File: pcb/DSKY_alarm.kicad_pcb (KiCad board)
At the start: 4 copper layers, 57.8 x 101.6 mm, 88 parts, among them IC3 ATSAMD21E, SW1 reset, U1 AQY232SZ, U10 AQY232SZ, U11 AQY232SZ, U12 AQY232SZ, U13 AQY232SZ, U14 AQY232SZ, U15 AP2112K-3.3, U2 AQY232SZ, U3 AQY232SZ, U4 AQY232SZ, U5 AQY232SZ, U6 AQY232SZ, U7 AQY232SZ, U8 AQY232SZ, X1 USB_MICRO_20329_V2_revised, u9 AQY232SZ

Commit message: Version 4 of the board
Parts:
- added NT1: Net-Tie_2, NetTie:NetTie-2_SMD_Pad0.5mm, F.Cu at (109.2, 146.7)
- LA11, LA12, LA13, LA21, LA22, LA23, LA31, LA32, LA33, LA41, LA42, LA43, LA51, LA52, LA53, LA61, LA62, LA63, LA71, LA72, LA73, LA81, LA82, LA83, LA91, LA92, LA93, LAA1, LAA2, LAA3, LAB1, LAB2, LAB3, LAC1, LAC2, LAC3, LAD1, LAD2, LAD3, LAE1, LAE2, LAE3: footprint Trinket M0 rev D:VCC7216-ND -> Trinket M0 rev D:VCC7265
- X1: value USB_MICRO_20329_V2_revised -> Molex 105133 USB; footprint Trinket M0 rev D:4UCONN_20329_V2_revised -> libraries:MOLEX_105133-0001
- moved X1 66.8 mm to (109.2, 138.4), turned to 0 degrees
- moved REF** 23.7 mm to (109.2, 130.8)
- moved R7 3.24 mm to (118.9, 135.3)
- moved U7 3.24 mm to (126.4, 136.5)
- moved R14 2.54 mm to (101.6, 135.9), turned to 180 degrees
- moved U14 2.54 mm to (94.0, 137.2)
- moved SWC1 1.27 mm to (87.6, 108.6)
- moved SWD1 1.27 mm to (84.5, 108.6)
- moved LA12 0.64 mm to (123.8, 53.3)
- moved LA42 0.64 mm to (123.8, 99.1)
- moved LA52 0.64 mm to (123.8, 114.3)
- moved LA62 0.64 mm to (123.8, 129.5)
- moved LA83 0.64 mm to (85.1, 53.3)
- moved LA93 0.64 mm to (85.1, 68.6)
- moved LAB3 0.64 mm to (85.1, 99.1)
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- renumbered u9 to U9
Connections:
- net +5V renamed VBAT
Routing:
- net VBUS: track 42.2 -> 81.6 mm, vias 2 -> 3
- net VBAT: track 539.1 -> 573.0 mm
- net GND: track 390.8 -> 415.0 mm, vias 0 -> 3
- net /D-: track 49.2 -> 30.4 mm, vias 2 -> 0
- net /D+: track 47.4 -> 29.7 mm, vias 2 -> 0
- net Net-(IC3-Pad31): track 37.6 -> 26.8 mm
- net LA6_PA22: track 32.9 -> 24.2 mm, vias 0 -> 2
- net LA5_PA19: track 26.3 -> 32.3 mm, vias 0 -> 2
- net LA3_PA04: track 20.7 -> 26.1 mm
- net Net-(IC3-Pad32): track 36.1 -> 32.1 mm
- net LA2_PA03: track 53.9 -> 56.8 mm, vias 2 -> 3
- net Net-(R6-Pad2): track 7.85 -> 5.10 mm, vias 2 -> 0
- net LA1_PA02: track 53.3 -> 50.5 mm
- net LA11_PA15: track 20.5 -> 18.0 mm
- net LA14_PA18: track 33.0 -> 30.7 mm, vias 2 -> 0
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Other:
- board text added: "DSKY Alarm Indicator, V4.0"
- board text removed: "DSKY Alarm Indicator, V3.0"

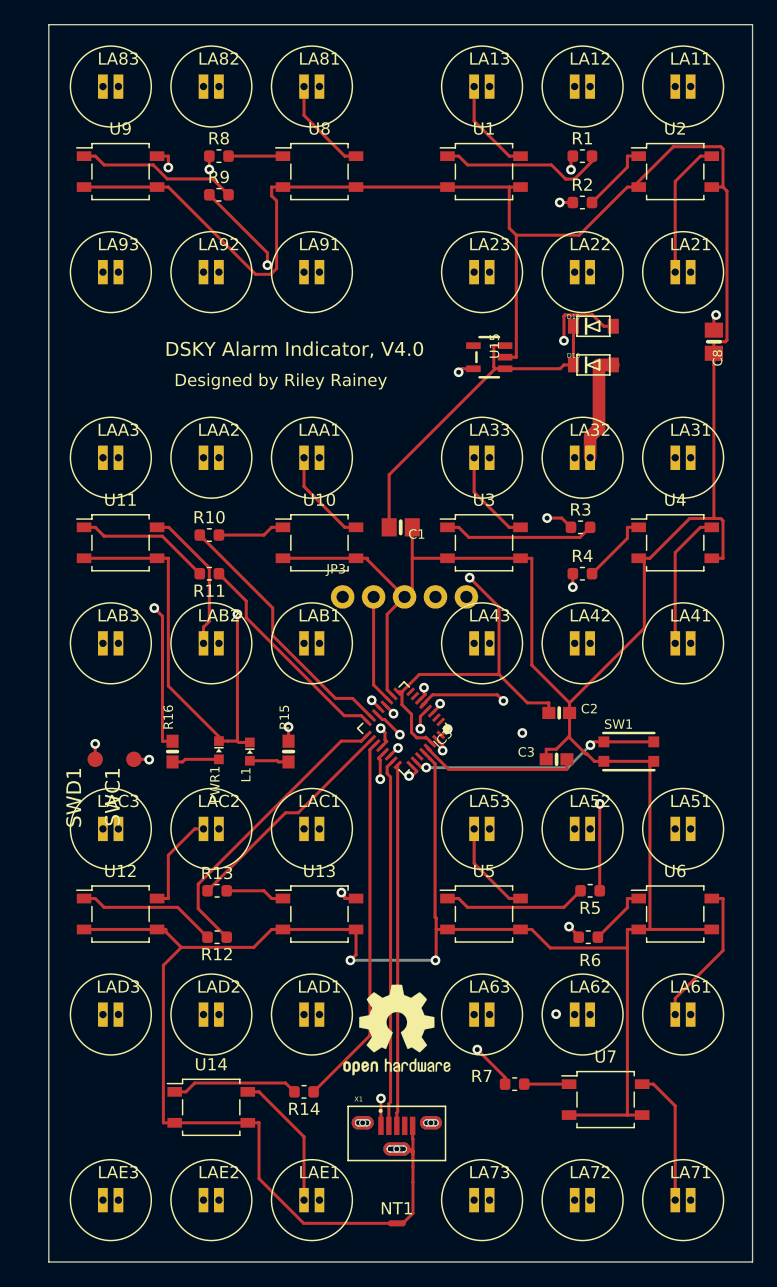
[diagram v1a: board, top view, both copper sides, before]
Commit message: Updated V4 board to a two layer design
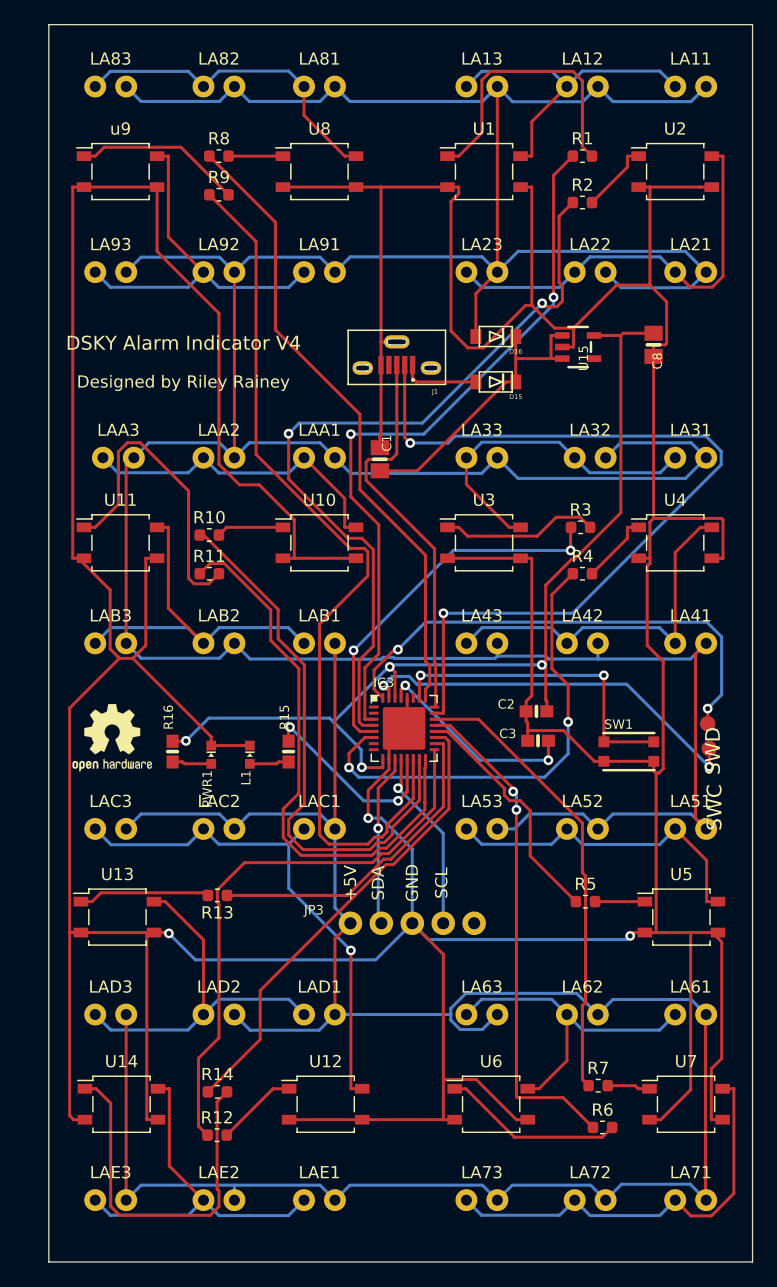
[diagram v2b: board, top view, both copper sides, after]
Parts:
- removed NT1: Net-Tie_2, NetTie:NetTie-2_SMD_Pad0.5mm
- removed the REF** at (109.2, 130.8)
- removed X1: Molex 105133 USB, libraries:MOLEX_105133-0001
- added J1: 105133-0001-MOLEX-USB, libraries:MOLEX_105133-0001, F.Cu at (109.2, 76.5)
- added REF**: OSHW-Logo2_7.3x6mm_SilkScreen, Symbol:OSHW-Logo2_7.3x6mm_SilkScreen, F.Cu at (85.9, 106.8)
- LA11, LA12, LA13, LA21, LA22, LA23, LA31, LA32, LA33, LA41, LA42, LA43, LA51, LA52, LA53, LA61, LA62, LA63, LA71, LA72, LA73, LA81, LA82, LA83, LA91, LA92, LA93, LAA1, LAA2, LAA3, LAB1, LAB2, LAB3, LAC1, LAC2, LAC3, LAD1, LAD2, LAD3, LAE1, LAE2, LAE3: footprint Trinket M0 rev D:VCC7265 -> Trinket M0 rev D:VCC7216-ND
- moved SWD 50.4 mm to (134.7, 105.7)
- moved SWC 47.3 mm to (134.9, 107.7)
- moved JP3 26.8 mm to (110.5, 122.0)
- moved U12 23.0 mm to (103.4, 136.9)
- moved U6 21.7 mm to (117.0, 136.9)
- moved U13 16.6 mm to (86.3, 121.5)
- moved R12 16.3 mm to (94.5, 139.4), turned to 0 degrees
- moved U5 16.2 mm to (132.6, 121.5)
- moved R6 15.7 mm to (126.1, 138.8)
- moved D15 9.23 mm to (117.3, 77.6), turned to 180 degrees
- moved D16 8.35 mm to (117.3, 73.9), turned to 180 degrees
- moved U14 7.37 mm to (86.6, 136.9)
- moved U15 7.35 mm to (124.1, 74.7), turned to 270 degrees
- moved R14 7.11 mm to (94.5, 135.9), turned to 0 degrees
- moved R7 6.86 mm to (125.8, 135.4)
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- renumbered SWC1 to SWC, SWD1 to SWD, U9 to u9
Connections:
- net VBAT renamed +5V
- IC3 pad 1: (no net) -> Net-(IC3-Pad1)
- IC3 pad 2: (no net) -> Net-(IC3-Pad2)
- IC3 pad 27: (no net) -> Net-(IC3-Pad27)
- IC3 pad 7: (no net) -> /D4_A2_PA06_TXD_MOSI
- IC3 pad 8: (no net) -> /D3_A3_PA07_RXD_SCK
- JP3 pad 5: (no net) -> Net-(JP3-Pad5)
- U15 pad 4: (no net) -> Net-(U15-Pad4)
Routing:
- net GND: track 415.0 -> 520.5 mm
- net +5V: track 573.0 -> 497.6 mm
- net VBUS: track 81.6 -> 6.40 mm, vias 3 -> 0
- net /D-: track 30.4 -> 70.8 mm, vias 0 -> 2
- net 3.3V: track 111.6 -> 81.9 mm
- net LA11_PA15: track 18.0 -> 45.9 mm
- net LA10_PA14: track 21.7 -> 45.6 mm
- net LA12_PA16: track 24.3 -> 46.6 mm
- net LA4_P05: track 18.9 -> 38.9 mm
- net Net-(R14-Pad2): track 10.4 -> 30.4 mm
- net LA9_PA11: track 53.8 -> 73.4 mm, vias 2 -> 0
- net LA6_PA22: track 24.2 -> 41.3 mm
- net Net-(R11-Pad2): track 11.1 -> 25.8 mm
- net Net-(LAC1-Pad1): track 28.2 -> 42.4 mm, vias 0 -> 1
- net LA5_PA19: track 32.3 -> 19.9 mm, vias 2 -> 0
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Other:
- copper layers 4 -> 2
- net class PWR: trace_width 1.0414 -> 0.25
- board text added: "+5V"
- board text added: "DSKY Alarm Indicator V4"
- board text added: "GND"
- board text added: "SCL"
- board text added: "SDA"
- board text removed: "DSKY Alarm Indicator, V4.0"
